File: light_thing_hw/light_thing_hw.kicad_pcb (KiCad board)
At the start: 2 copper layers, 50 x 50 mm, 60 parts, among them J1 CONNECTORS, J2 Li-Ion Battery, J3 ADDR_LED_PANEL_1_CONNECTORS, J4 ADDR_LED_PANEL_2_CONNECTORS, J5 MIC_CONN, Q1 MMBF170, Q2 BSS83P, SW1 ST_USER_BUTTON1, SW2 ST_RESET_BUTTON, U1 BC832-V1, U2 LSM6DS3, U3 MCP73833T-FCI_UN, U4 LMR62421XMF, U5 LP38511MRX-ADJ_NOPB, U6 STM32L476RGTx

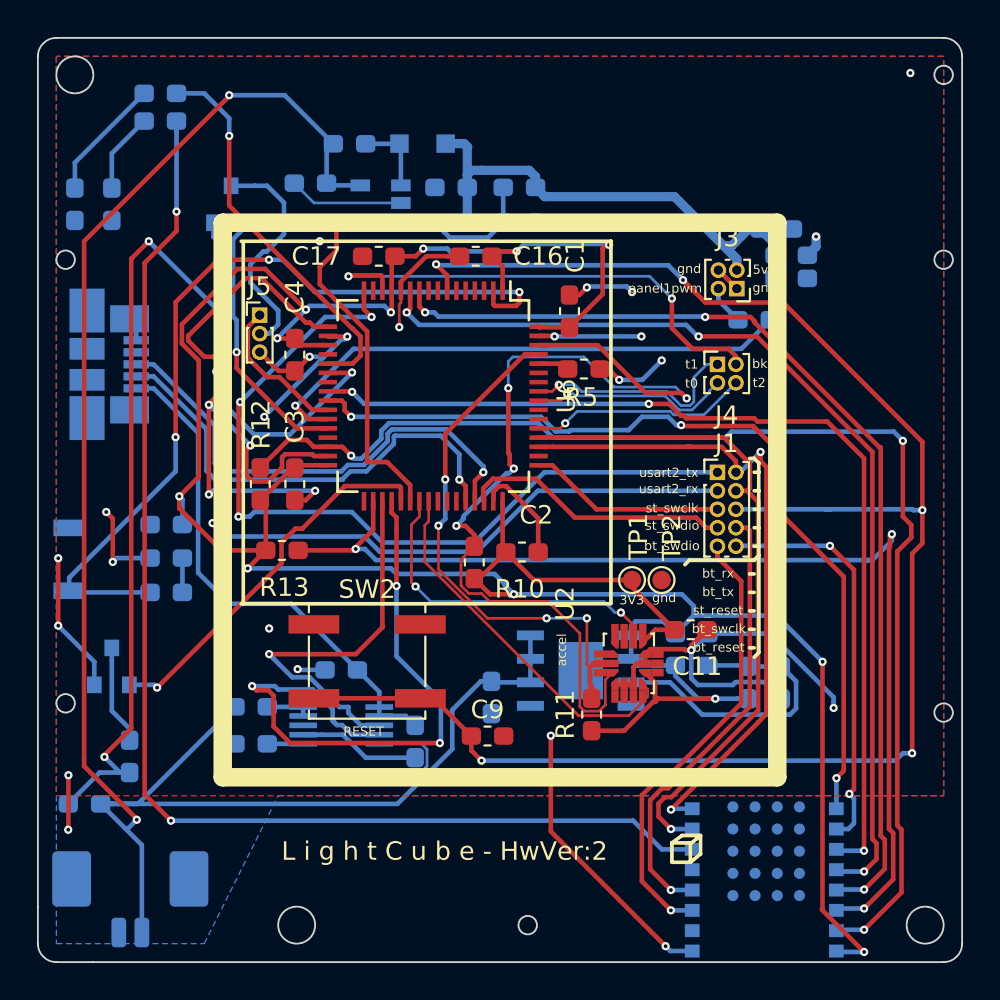
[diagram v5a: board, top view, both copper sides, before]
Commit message: picked new reset button and diode footprint
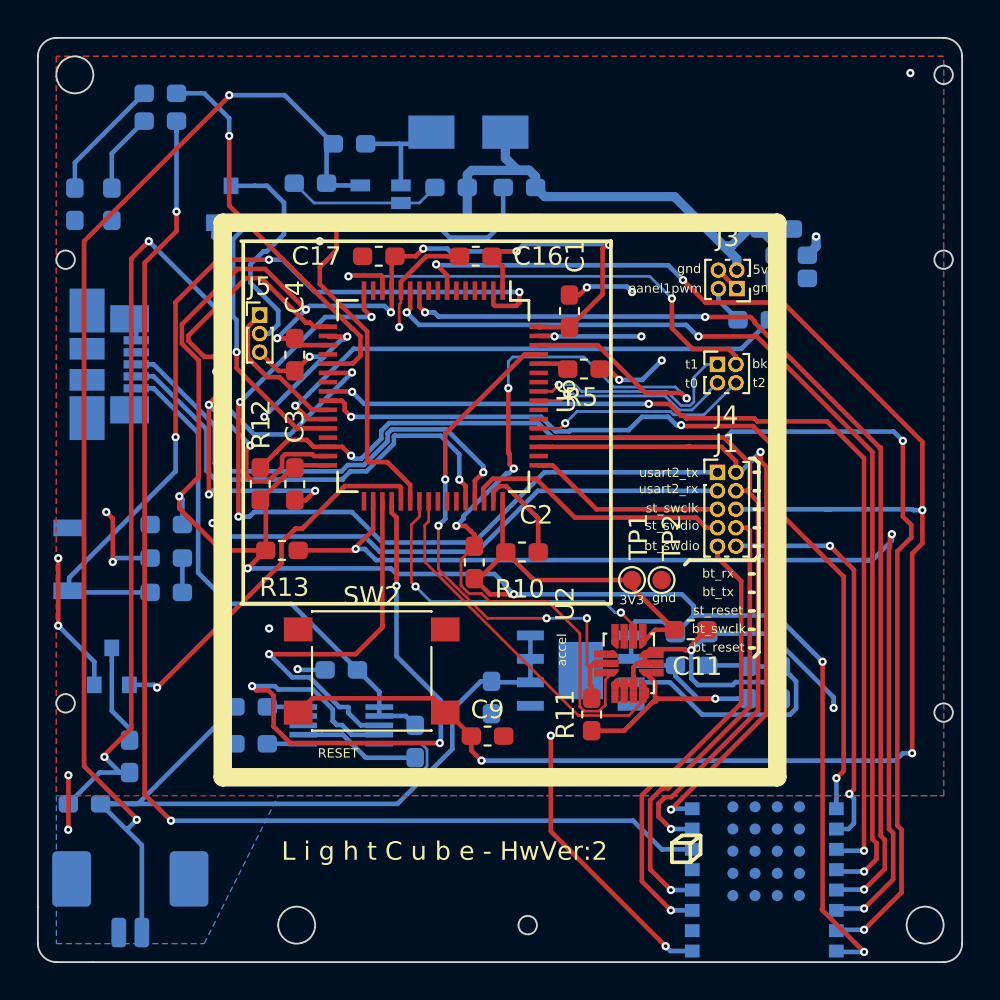
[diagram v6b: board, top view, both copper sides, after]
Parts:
- D1: footprint Diode_SMD:D_SOD-323_HandSoldering -> Diode_SMD:D_SMA
- SW2: footprint Button_Switch_SMD:SW_SPST_EVPBF -> Button_Switch_SMD:SW_SPST_PTS645
- moved D1 2.56 mm to (142.8, 70.3)
- moved SW2 0.58 mm to (137.6, 99.5)
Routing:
- net GND: track 134.5 -> 136.7 mm
- net RESET: track 93.8 -> 95.0 mm
- net Net-(D1-Pad2): track 4.12 -> 5.11 mm
